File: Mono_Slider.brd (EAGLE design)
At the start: 80 x 80 mm, 6 parts

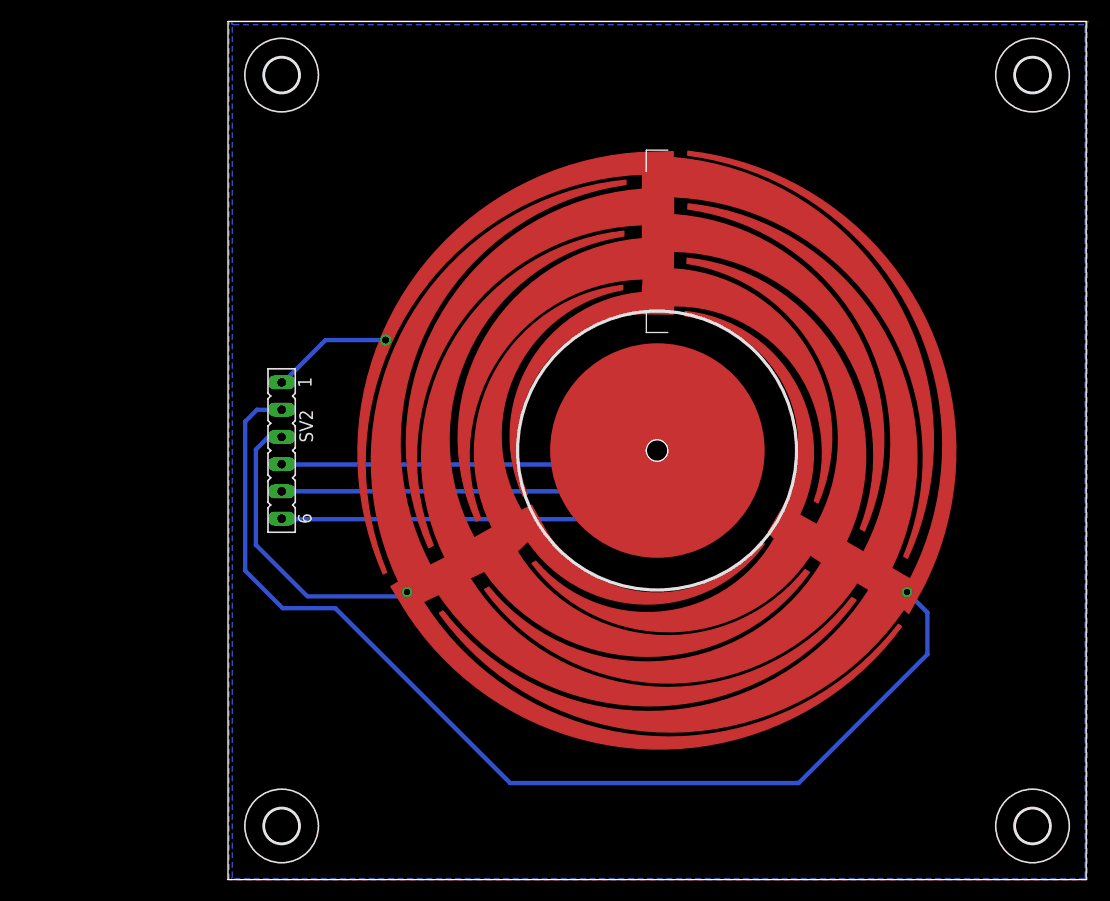
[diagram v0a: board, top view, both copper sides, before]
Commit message: Made slider smaller.
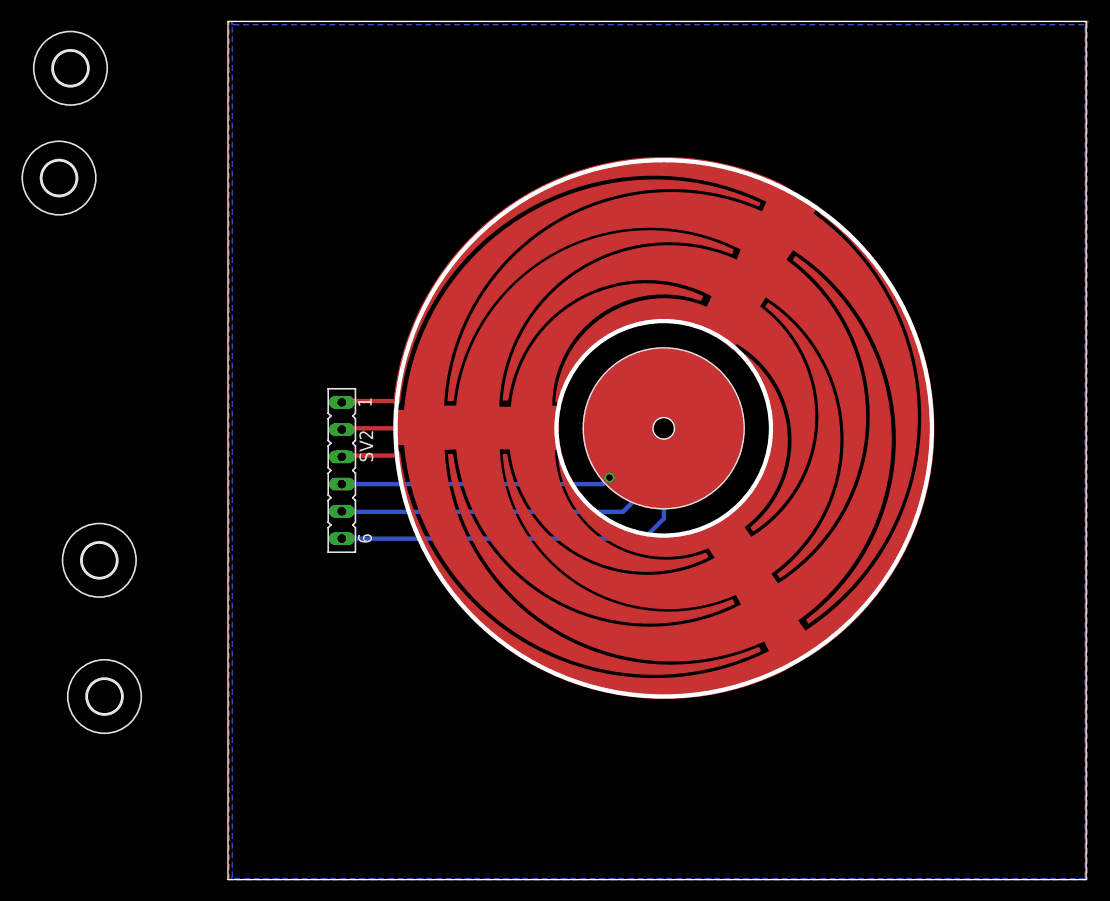
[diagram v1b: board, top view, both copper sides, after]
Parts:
- SL1: device SLIDER:SLIDER -> SLIDER:SLIDER_SMALL
- moved H3 91.3 mm to (-15.8, 65.4)
- moved H4 90.5 mm to (-12.0, 29.8)
- moved H2 20.4 mm to (-11.5, 17.1)
- moved H1 19.7 mm to (-14.7, 75.6)
- moved SV2 5.91 mm to (10.6, 38.1)
- moved SL1 2.16 mm to (40.6, 42.1), turned to 90 degrees
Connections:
- removed net N$13: SL1.SP3, SV2.2
- removed net N$6: SL1.SP2, SV2.3
- removed net N$7: SL1.SP1, SV2.1
- new net SP1: SL1.SP1, SV2.3
- new net SP2: SL1.SP2, SV2.2
- new net SP3: SL1.SP3, SV2.1
- net CT: now also SL1.CP; no longer SL1.CT
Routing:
- net N$12: track 101.2 -> 0.00 mm
- net N$4: track 94.1 -> 0.00 mm, vias 3 -> 0
- net N$2: track 41.7 -> 0.00 mm
- net GND: track 0.00 -> 38.5 mm
- net N$1: track 37.5 -> 0.00 mm
- net 3V3: track 0.00 -> 37.4 mm
- net N$3: track 29.0 -> 0.00 mm
- net CT: track 0.00 -> 26.0 mm, vias 0 -> 1
- net N$15: track 18.6 -> 0.00 mm
- net N$9: track 9.22 -> 0.00 mm
- net N$5: track 7.50 -> 0.00 mm
- net N$11: track 6.88 -> 0.00 mm
- net SP1: track 0.00 -> 2.19 mm
- net SP3: track 0.00 -> 2.19 mm
- net SP2: track 0.00 -> 2.19 mm
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
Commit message: Made pcb smaller to fit in case..
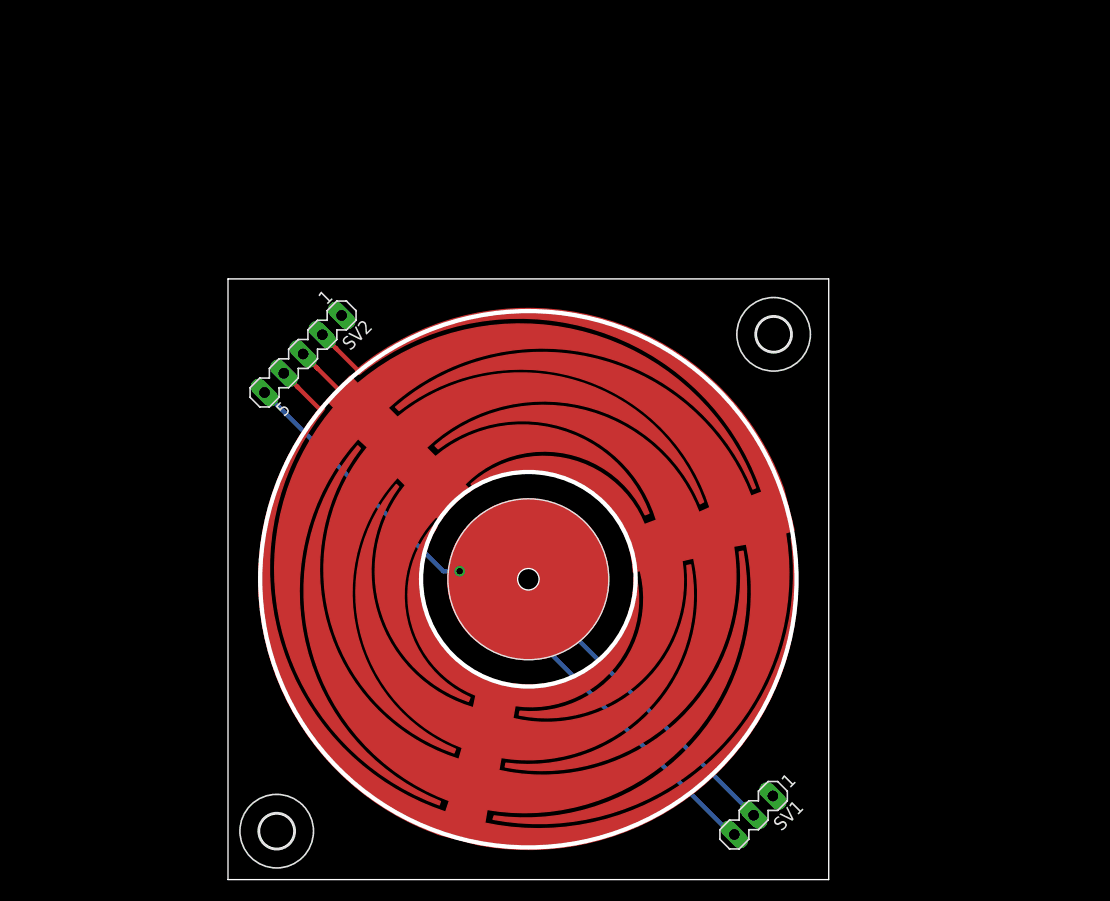
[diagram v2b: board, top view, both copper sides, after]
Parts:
- removed H3, H4: MOUNT-HOLE3.2, holes:3,2
- added SV1: (no value), con-lstb:MA03-1
- SV2: value FemaleHeader -> (none); device con-lsta:FE06 -> con-lstb:MA05-1
- moved H1 70.1 mm to (50.9, 50.8)
- moved H2 20.4 mm to (4.54, 4.51)
- moved SL1 18.9 mm to (28.0, 28.0), turned to 45 degrees
- moved SV2 11.4 mm to (7.00, 49.0), turned to 225 degrees
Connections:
- removed net 3V3: SL1.A, SV2.6
- removed net CT: SL1.CP, SV2.4
- removed net SP1: SL1.SP1, SV2.3
- removed net SP2: SL1.SP2, SV2.2
- removed net SP3: SL1.SP3, SV2.1
- new net N$1: SL1.A, SV1.3
- new net N$2: SL1.K, SV1.2
- new net N$3: SL1.CP, SV2.5
- new net N$4: SL1.SP1, SV2.4
- new net N$5: SL1.SP2, SV2.3
- new net N$6: SL1.SP3, SV2.2
- net GND: now also SV1.1, SV2.1; no longer SL1.K, SV2.5
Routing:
- net GND: track 38.5 -> 0.00 mm
- net 3V3: track 37.4 -> 0.00 mm
- net N$1: track 0.00 -> 32.2 mm
- net N$2: track 0.00 -> 31.4 mm
- net CT: track 26.0 -> 0.00 mm, vias 1 -> 0
- net N$3: track 0.00 -> 25.3 mm, vias 0 -> 1
- net SP1: track 2.19 -> 0.00 mm
- net SP3: track 2.19 -> 0.00 mm
- net SP2: track 2.19 -> 0.00 mm
- net N$5: track 0.00 -> 2.10 mm
- net N$6: track 0.00 -> 1.93 mm
- net N$4: track 0.00 -> 1.93 mm
- removed copper zone on layer 1, net GND
- removed copper zone on layer 16, net GND
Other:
- board size 80 x 80 mm -> 56 x 56 mm
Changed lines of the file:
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@@
 <board>
 <plain>
-<wire x1="0" y1="0" x2="80" y2="0" width="0" layer="20"/>
-<wire x1="80" y1="0" x2="80" y2="80" width="0" layer="20"/>
-<wire x1="80" y1="80" x2="0" y2="80" width="0" layer="20"/>
-<wire x1="0" y1="80" x2="0" y2="0" width="0" layer="20"/>
+<wire x1="0" y1="0" x2="56" y2="0" width="0" layer="20"/>
+<wire x1="56" y1="0" x2="56" y2="56" width="0" layer="20"/>
+<wire x1="56" y1="56" x2="0" y2="56" width="0" layer="20"/>
+<wire x1="0" y1="56" x2="0" y2="0" width="0" layer="20"/>
 <dimension x1="0" y1="0" x2="0" y2="80.01" x3="-5.08" y3="40.005" textsize="1.778" layer="47"/>
 <dimension x1="0" y1="80" x2="80.03" y2="80.01" x3="40.01420625" y3="86.355" textsize="1.778" layer="47"/>
@@
 </autorouter>
 <elements>
-<element name="H1" library="holes" package="3,2" value="MOUNT-HOLE3.2" x="-14.685" y="75.635"/>
-<element name="H2" library="holes" package="3,2" value="MOUNT-HOLE3.2" x="-11.51" y="17.065"/>
-<element name="H3" library="holes" package="3,2" value="MOUNT-HOLE3.2" x="-15.75" y="65.4"/>
-<element name="H4" library="holes" package="3,2" value="MOUNT-HOLE3.2" x="-11.995" y="29.765"/>
-<element name="SV2" library="con-lsta" package="FE06" value="FemaleHeader" x="10.61" y="38.14" rot="R270">
-<attribute name="MPN" value="" x="10.61" y="38.14" size="1.778" layer="27" rot="R270" display="off"/>
-<attribute name="OC_FARNELL" value="unknown" x="10.61" y="38.14" size="1.778" layer="27" rot="R270" display="off"/>
-<attribute name="OC_NEWARK" value="unknown" x="10.61" y="38.14" size="1.778" layer="27" rot="R270" display="off"/>
-<attribute name="MF" value="" x="10.61" y="38.14" size="1.778" layer="27" rot="R270" display="off"/>
+<element name="H1" library="holes" package="3,2" value="MOUNT-HOLE3.2" x="50.865" y="50.835"/>
+<element name="H2" library="holes" package="3,2" value="MOUNT-HOLE3.2" x="4.54" y="4.515"/>
+<element name="SL1" library="SLIDER" package="SLIDER_SMALL" value="SLIDER" x="28" y="28" rot="R45"/>
+<element name="SV1" library="con-lstb" package="MA03-1" value="" x="49" y="6" rot="R225">
+<attribute name="OC_NEWARK" value="unknown" x="49" y="6" size="1.778" layer="27" rot="R225" display="off"/>
+<attribute name="MF" value="" x="49" y="6" size="1.778" layer="27" rot="R225" display="off"/>
+<attribute name="OC_FARNELL" value="unknown" x="49" y="6" size="1.778" layer="27" rot="R225" display="off"/>
+<attribute name="MPN" value="" x="49" y="6" size="1.778" layer="27" rot="R225" display="off"/>
 </element>
-<element name="SL1" library="SLIDER" package="SLIDER_SMALL" value="SLIDER" x="40.62" y="42.07" rot="R90"/>
+<element name="SV2" library="con-lstb" package="MA05-1" value="" x="7" y="49" rot="R225">
+<attribute name="OC_NEWARK" value="unknown" x="7" y="49" size="1.778" layer="27" rot="R225" display="off"/>
+<attribute name="MF" value="" x="7" y="49" size="1.778" layer="27" rot="R225" display="off"/>
+<attribute name="OC_FARNELL" value="unknown" x="7" y="49" size="1.778" layer="27" rot="R225" display="off"/>
+<attribute name="MPN" value="" x="7" y="49" size="1.778" layer="27" rot="R225" display="off"/>
+</element>
 </elements>
 <signals>
-<signal name="3V3">
-<contactref element="SV2" pad="6"/>
+<signal name="N$11">
+</signal>
+<signal name="N$1">
 <contactref element="SL1" pad="A"/>
-<wire x1="40.62" y1="40.27" x2="40.64" y2="40.25" width="0.4064" layer="16"/>
-<wire x1="40.64" y1="40.25" x2="40.64" y2="33.655" width="0.4064" layer="16"/>
-<wire x1="40.64" y1="33.655" x2="38.775" y2="31.79" width="0.4064" layer="16"/>
-<wire x1="38.775" y1="31.79" x2="10.61" y2="31.79" width="0.4064" layer="16"/>
+<contactref element="SV1" pad="3"/>
+<wire x1="26.72720625" y1="26.72720625" x2="26.72720625" y2="26.72279375" width="0.4064" layer="16"/>
+<wire x1="26.72720625" y1="26.72279375" x2="28.7" y2="24.75" width="0.4064" layer="16"/>
+<wire x1="28.7" y1="24.75" x2="28.7" y2="22.45" width="0.4064" layer="16"/>
+<wire x1="28.7" y1="22.45" x2="47.45" y2="3.7" width="0.4064" layer="16"/>
+<wire x1="47.45" y1="3.7" x2="47.45" y2="3.95789375" width="0.4064" layer="16"/>
+<wire x1="47.45" y1="3.95789375" x2="47.203946875" y2="4.203946875" width="0.4064" layer="16"/>
+</signal>
+<signal name="N$2">
+<contactref element="SL1" pad="K"/>
+<contactref element="SV1" pad="2"/>
+<wire x1="29.272790625" y1="29.272790625" x2="29.277209375" y2="29.272790625" width="0.4064" layer="16"/>
+<wire x1="29.277209375" y1="29.272790625" x2="31.5" y2="27.05" width="0.4064" layer="16"/>
+<wire x1="31.5" y1="27.05" x2="31.5" y2="23.5" width="0.4064" layer="16"/>
+<wire x1="31.5" y1="23.5" x2="49" y2="6" width="0.4064" layer="16"/>
 </signal>
 <signal name="GND">
+<contactref element="SV1" pad="1"/>
+<contactref element="SV2" pad="1"/>
+<wire x1="50.79605" y1="7.79605" x2="10.5921" y2="52.5921" width="0" layer="19" extent="1-1"/>
+</signal>
+<signal name="N$3">
+<contactref element="SL1" pad="CP"/>
 <contactref element="SV2" pad="5"/>
-<polygon width="0.4064" layer="16" pour="hatch" isolate="1.27">
-<vertex x="0.3" y="79.9"/>
-<vertex x="0.5" y="79.7"/>
-<vertex x="80.1" y="79.7"/>
-<vertex x="79.9" y="79.5"/>
-<vertex x="79.9" y="0.1"/>
-<vertex x="0.3" y="0.1"/>
-<vertex x="0.4" y="0.2"/>
-<vertex x="0.4" y="79.7"/>
-</polygon>
-<polygon width="0.4064" layer="1" pour="hatch" isolate="1.27">
-<vertex x="0.1" y="80"/>
-<vertex x="80.2" y="80"/>
-<vertex x="80.1" y="79.9"/>
-<vertex x="80.1" y="0"/>
-<vertex x="0.1" y="0"/>
-</polygon>
-<contactref element="SL1" pad="K"/>
-<wire x1="40.62" y1="43.87" x2="40.565" y2="43.815" width="0.4064" layer="16"/>
-<wire x1="40.565" y1="43.815" x2="38.735" y2="43.815" width="0.4064" layer="16"/>
-<wire x1="38.735" y1="43.815" x2="38.1" y2="43.18" width="0.4064" layer="16"/>
-<wire x1="38.1" y1="43.18" x2="38.1" y2="35.56" width="0.4064" layer="16"/>
-<wire x1="38.1" y1="35.56" x2="36.83" y2="34.29" width="0.4064" layer="16"/>
-<wire x1="36.83" y1="34.29" x2="10.65" y2="34.29" width="0.4064" layer="16"/>
-<wire x1="10.65" y1="34.29" x2="10.61" y2="34.33" width="0.4064" layer="16"/>
-</signal>
-<signal name="CT">
+<wire x1="21.71381875" y1="28.898025" x2="21.631975" y2="28.718025" width="0.4064" layer="1"/>
+<wire x1="21.631975" y1="28.718025" x2="21.6" y2="28.75" width="0.4064" layer="1"/>
+<via x="21.6" y="28.75" extent="1-16" drill="0.6" shape="octagon"/>
+<wire x1="21.6" y1="28.75" x2="20.06579375" y2="28.75" width="0.4064" layer="16"/>
+<wire x1="20.06579375" y1="28.75" x2="3.407896875" y2="45.407896875" width="0.4064" layer="16"/>
+</signal>
+<signal name="N$4">
+<contactref element="SL1" pad="SP1"/>
 <contactref element="SV2" pad="4"/>
-<contactref element="SL1" pad="CP"/>
-<wire x1="35.54" y1="38.26" x2="35.56" y2="38.24" width="0.4064" layer="1"/>
-<wire x1="35.56" y1="38.24" x2="35.56" y2="37.465" width="0.4064" layer="1"/>
-<via x="35.56" y="37.465" extent="1-16" drill="0.6" shape="octagon"/>
-<wire x1="35.56" y1="37.465" x2="34.965" y2="36.87" width="0.4064" layer="16"/>
-<wire x1="34.965" y1="36.87" x2="10.61" y2="36.87" width="0.4064" layer="16"/>
-</signal>
-<signal name="N$11">
-</signal>
-<signal name="SP1">
+<wire x1="5.203946875" y1="47.203946875" x2="6.447384375" y2="45.960509375" width="0.4064" layer="1"/>
+<wire x1="6.567384375" y1="45.840509375" x2="6.447384375" y2="45.960509375" width="0.4064" layer="1"/>
+</signal>
+<signal name="N$5">
+<contactref element="SL1" pad="SP2"/>
 <contactref element="SV2" pad="3"/>
-<contactref element="SL1" pad="SP1"/>
-<wire x1="12.68" y1="39.53" x2="10.61" y2="39.53" width="0.4064" layer="1"/>
-<wire x1="10.61" y1="39.53" x2="10.61" y2="39.41" width="0.4064" layer="1"/>
-</signal>
-<signal name="SP2">
+<wire x1="7" y1="49" x2="8.363434375" y2="47.636565625" width="0.4064" layer="1"/>
+<wire x1="8.363434375" y1="47.636565625" x2="8.243434375" y2="47.7565625" width="0.4064" layer="1"/>
+</signal>
+<signal name="N$6">
+<contactref element="SL1" pad="SP3"/>
 <contactref element="SV2" pad="2"/>
-<contactref element="SL1" pad="SP2"/>
-<wire x1="12.68" y1="42.07" x2="10.61" y2="42.07" width="0.4064" layer="1"/>
-<wire x1="10.61" y1="42.07" x2="10.61" y2="41.95" width="0.4064" layer="1"/>
-</signal>
-<signal name="SP3">
-<contactref element="SV2" pad="1"/>
-<contactref element="SL1" pad="SP3"/>
-<wire x1="12.68" y1="44.61" x2="10.61" y2="44.61" width="0.4064" layer="1"/>
-<wire x1="10.61" y1="44.61" x2="10.61" y2="44.49" width="0.4064" layer="1"/>
+<wire x1="8.79605" y1="50.79605" x2="10.0394875" y2="49.5526125" width="0.4064" layer="1"/>
+<wire x1="10.1594875" y1="49.4326125" x2="10.0394875" y2="49.5526125" width="0.4064" layer="1"/>
 </signal>
 </signals>
